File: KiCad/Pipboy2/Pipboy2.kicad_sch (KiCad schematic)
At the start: 12 parts, among them J1 Battery Socket, J2 LCD Socket, SW1 SW_SPST, SW2 SW_SPST

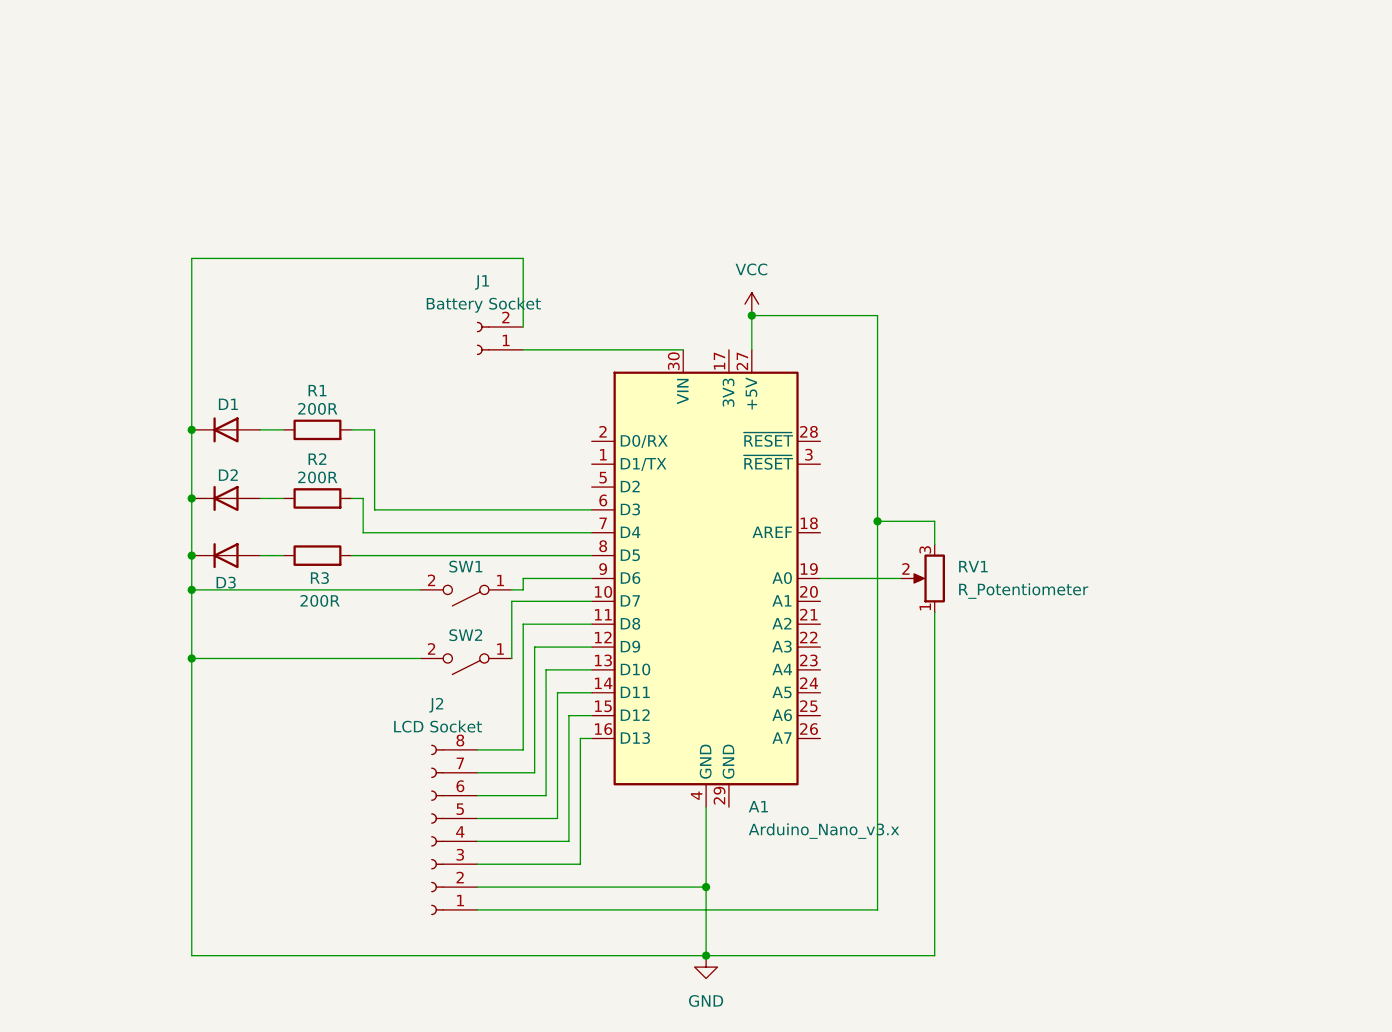
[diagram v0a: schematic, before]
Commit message: Added voltage reg, power button, updated pcb editor scheme
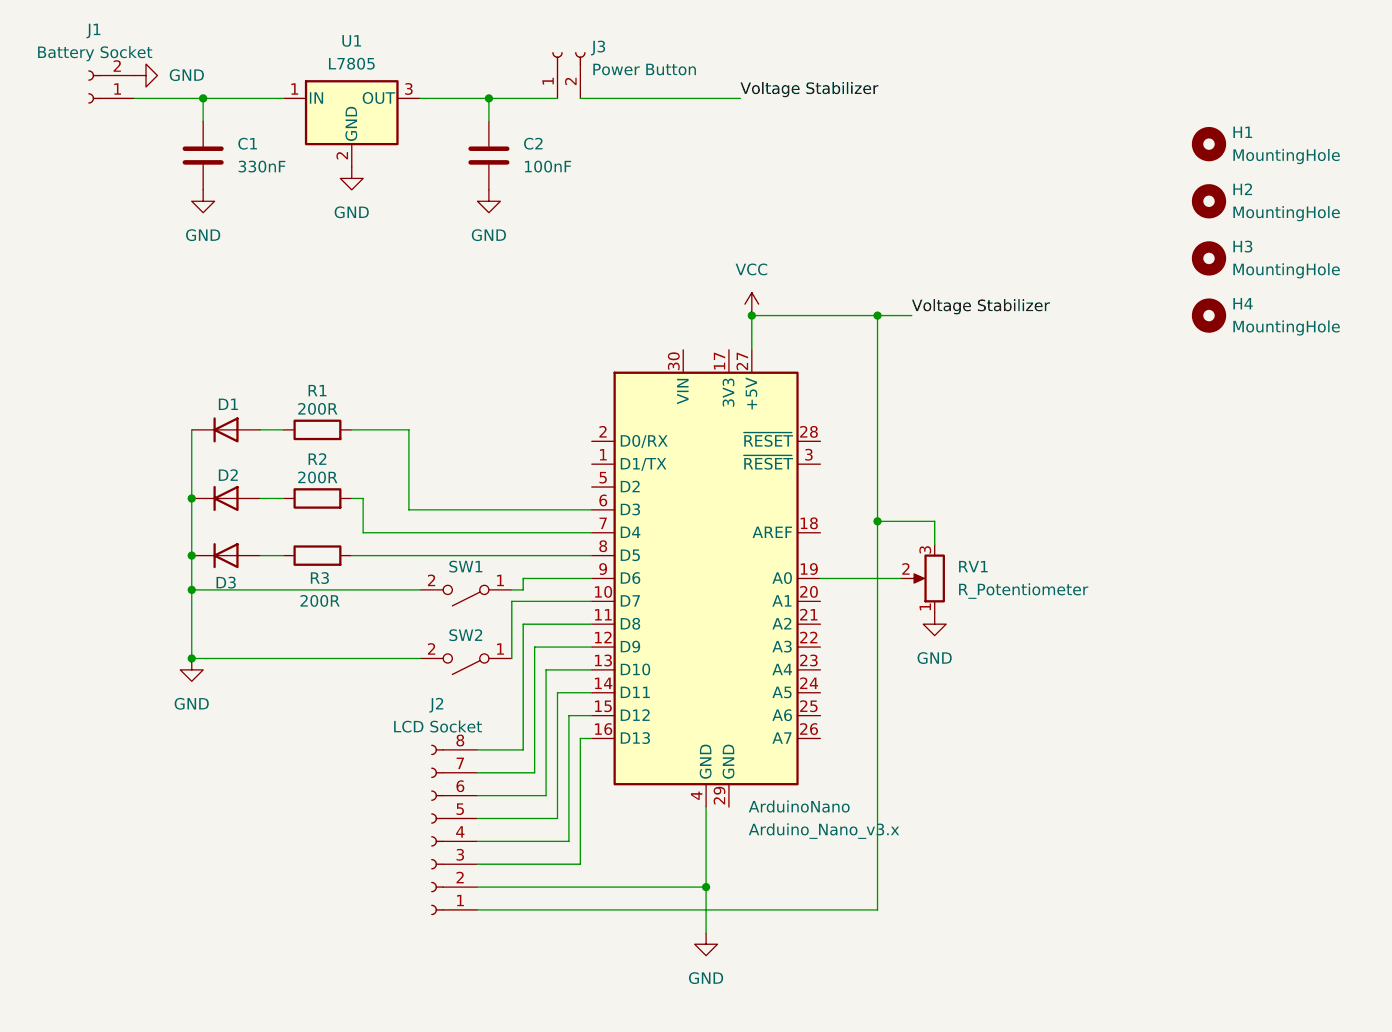
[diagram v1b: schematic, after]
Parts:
- added C1: 330nF, Capacitor_THT:CP_Axial_L10.0mm_D4.5mm_P15.00mm_Horizontal, symbol Device:C
- added C2: 100nF, Capacitor_THT:CP_Axial_L10.0mm_D4.5mm_P15.00mm_Horizontal, symbol Device:C
- added H1, H2, H3, H4: MountingHole, MountingHole:MountingHole_3.2mm_M3, symbol Mechanical:MountingHole
- added J3: Power Button, Connector_PinHeader_1.00mm:PinHeader_1x02_P1.00mm_Vertical, symbol Connector:Conn_01x02_Socket
- added U1: L7805, Package_TO_SOT_THT:TO-220-3_Vertical, symbol Regulator_Linear:L7805
- renumbered A1 to ArduinoNano
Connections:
- net GND: now also C1.2, C2.2, U1.2 (GND)
- net VCC: now also J3.2 (Pin_2)
- net at ArduinoNano.30 (VIN): no longer J1.1 (Pin_1)
- new net: C1.1, J1.1 (Pin_1), U1.1 (IN)
- new net: C2.1, J3.1 (Pin_1), U1.3 (OUT)
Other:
- moved on the sheet: J1

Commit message: Removed plate violations
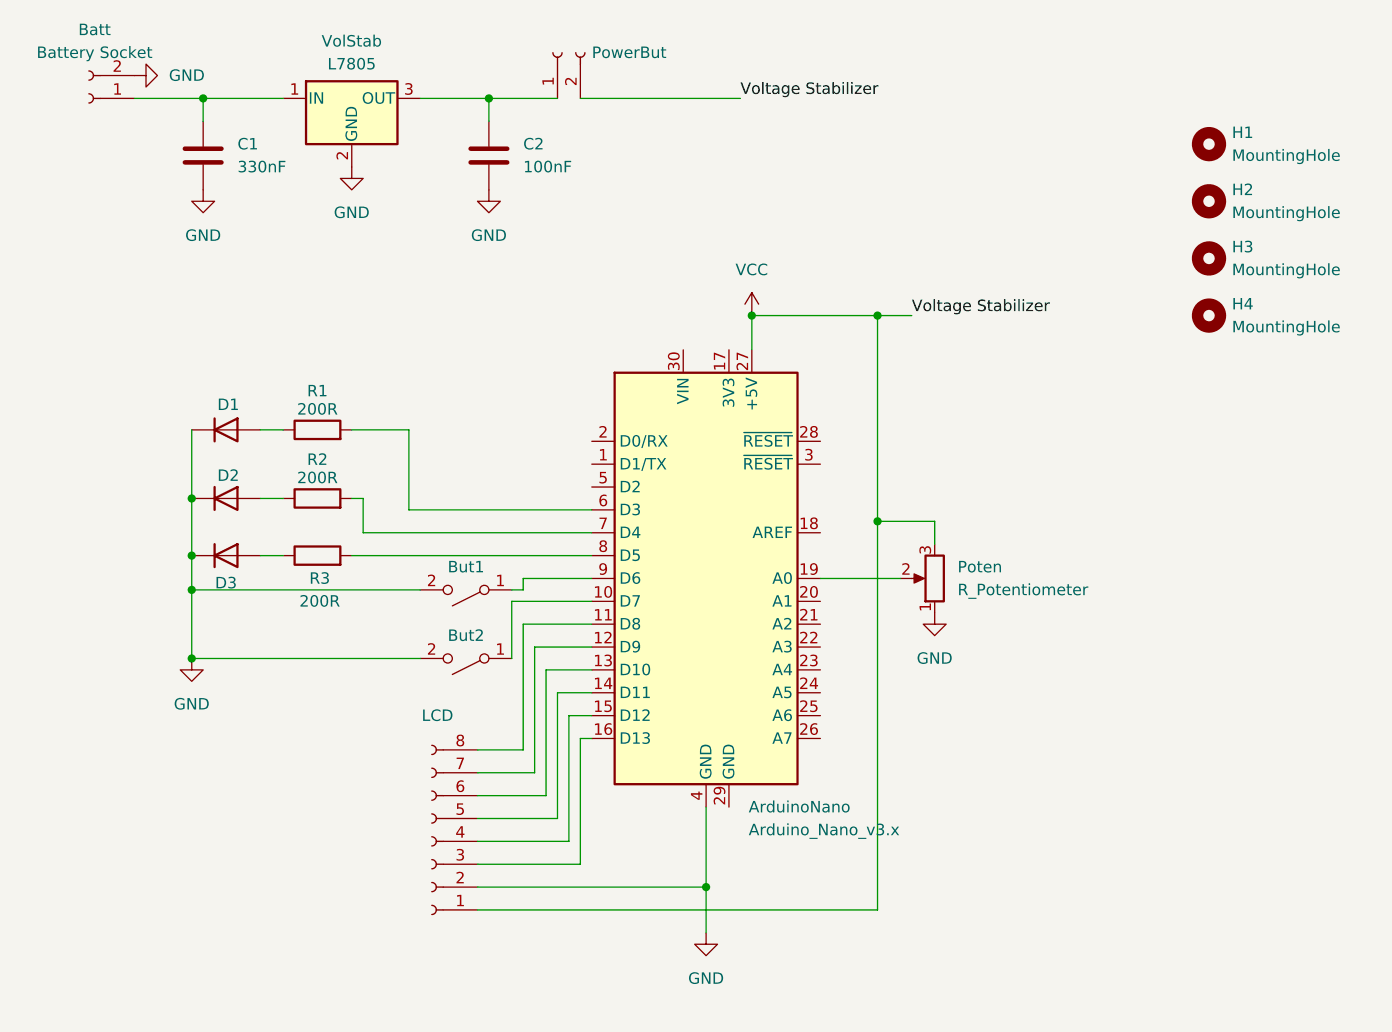
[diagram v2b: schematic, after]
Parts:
- LCD: renamed from J2; value LCD Socket -> ~
- PowerBut: renamed from J3; value Power Button -> ~; footprint Connector_PinHeader_1.00mm:PinHeader_1x02_P1.00mm_Vertical -> Connector_PinHeader_2.54mm:PinHeader_1x02_P2.54mm_Vertical
- renumbered J1 to Batt, SW1 to But1, SW2 to But2, RV1 to Poten, U1 to VolStab
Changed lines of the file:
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@@
 		(dnp no)
 		(fields_autoplaced yes)
-		(property "Reference" "U1"
+		(property "Reference" "VolStab"
 			(at 143.51 36.83 0)
 			(effects
@@
 			(project ""
 				(path "/e5f66db8-0cc8-44f6-bfd7-85690320585e"
-					(reference "U1")
+					(reference "VolStab")
 					(unit 1)
 				)
@@
 		(dnp no)
 		(fields_autoplaced yes)
-		(property "Reference" "SW2"
+		(property "Reference" "But2"
 			(at 156.21 102.87 0)
 			(effects
@@
 			(project "Pipboy2"
 				(path "/e5f66db8-0cc8-44f6-bfd7-85690320585e"
-					(reference "SW2")
+					(reference "But2")
 					(unit 1)
 				)
@@
 		(dnp no)
 		(fields_autoplaced yes)
-		(property "Reference" "J2"
-			(at 153.035 110.49 0)
-			(effects
-				(font
-					(size 1.27 1.27)
-				)
-			)
-		)
-		(property "Value" "LCD Socket"
+		(property "Reference" "LCD"
+			(at 153.035 111.76 0)
+			(effects
+				(font
+					(size 1.27 1.27)
+				)
+			)
+		)
+		(property "Value" "~"
 			(at 153.035 113.03 0)
 			(effects
@@
 			(project ""
 				(path "/e5f66db8-0cc8-44f6-bfd7-85690320585e"
-					(reference "J2")
+					(reference "LCD")
 					(unit 1)
 				)
@@
 		(dnp no)
 		(fields_autoplaced yes)
-		(property "Reference" "J1"
+		(property "Reference" "Batt"
 			(at 114.935 35.56 0)
 			(effects
@@
 			(project ""
 				(path "/e5f66db8-0cc8-44f6-bfd7-85690320585e"
-					(reference "J1")
+					(reference "Batt")
 					(unit 1)
 				)
@@
 		(dnp no)
 		(fields_autoplaced yes)
-		(property "Reference" "RV1"
+		(property "Reference" "Poten"
 			(at 210.82 95.2499 0)
 			(effects
@@
 			(project ""
 				(path "/e5f66db8-0cc8-44f6-bfd7-85690320585e"
-					(reference "RV1")
+					(reference "Poten")
 					(unit 1)
 				)
@@
 		(dnp no)
 		(fields_autoplaced yes)
-		(property "Reference" "J3"
-			(at 170.18 37.4649 90)
+		(property "Reference" "PowerBut"
+			(at 170.18 38.0999 90)
 			(effects
 				(font
@@
 			)
 		)
-		(property "Value" "Power Button"
-			(at 170.18 40.0049 90)
+		(property "Value" "~"
+			(at 170.18 40.005 90)
 			(effects
 				(font
@@
 			)
 		)
-		(property "Footprint" "Connector_PinHeader_1.00mm:PinHeader_1x02_P1.00mm_Vertical"
+		(property "Footprint" "Connector_PinHeader_2.54mm:PinHeader_1x02_P2.54mm_Vertical"
 			(at 166.37 38.1 0)
 			(effects
@@
 			(project "Pipboy2"
 				(path "/e5f66db8-0cc8-44f6-bfd7-85690320585e"
-					(reference "J3")
+					(reference "PowerBut")
 					(unit 1)
 				)
@@
 		(dnp no)
 		(fields_autoplaced yes)
-		(property "Reference" "SW1"
+		(property "Reference" "But1"
 			(at 156.21 95.25 0)
 			(effects
@@
 			(project ""
 				(path "/e5f66db8-0cc8-44f6-bfd7-85690320585e"
-					(reference "SW1")
-					(unit 1)
-				)
+					(reference "But1")
+					(unit 1)
+				)

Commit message: Exported steps
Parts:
- renumbered ArduinoNano to ArduinoNano1, Batt to Batt1, LCD to LCD1, Poten to Poten1, PowerBut to PowerBut1, VolStab to VolStab1
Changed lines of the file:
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@@
 		(dnp no)
 		(fields_autoplaced yes)
-		(property "Reference" "ArduinoNano"
+		(property "Reference" "ArduinoNano1"
 			(at 187.6141 121.92 0)
 			(effects
@@
 			(project ""
 				(path "/e5f66db8-0cc8-44f6-bfd7-85690320585e"
-					(reference "ArduinoNano")
+					(reference "ArduinoNano1")
 					(unit 1)
 				)
@@
 		(dnp no)
 		(fields_autoplaced yes)
-		(property "Reference" "VolStab"
+		(property "Reference" "VolStab1"
 			(at 143.51 36.83 0)
 			(effects
@@
 			(project ""
 				(path "/e5f66db8-0cc8-44f6-bfd7-85690320585e"
-					(reference "VolStab")
+					(reference "VolStab1")
 					(unit 1)
 				)
@@
 		(dnp no)
 		(fields_autoplaced yes)
-		(property "Reference" "LCD"
+		(property "Reference" "LCD1"
 			(at 153.035 111.76 0)
 			(effects
@@
 			(project ""
 				(path "/e5f66db8-0cc8-44f6-bfd7-85690320585e"
-					(reference "LCD")
+					(reference "LCD1")
 					(unit 1)
 				)
@@
 		(dnp no)
 		(fields_autoplaced yes)
-		(property "Reference" "Batt"
+		(property "Reference" "Batt1"
 			(at 114.935 35.56 0)
 			(effects
@@
 			(project ""
 				(path "/e5f66db8-0cc8-44f6-bfd7-85690320585e"
-					(reference "Batt")
+					(reference "Batt1")
 					(unit 1)
 				)
@@
 		(dnp no)
 		(fields_autoplaced yes)
-		(property "Reference" "Poten"
+		(property "Reference" "Poten1"
 			(at 210.82 95.2499 0)
 			(effects
@@
 			(project ""
 				(path "/e5f66db8-0cc8-44f6-bfd7-85690320585e"
-					(reference "Poten")
+					(reference "Poten1")
 					(unit 1)
 				)
@@
 		(dnp no)
 		(fields_autoplaced yes)
-		(property "Reference" "PowerBut"
+		(property "Reference" "PowerBut1"
 			(at 170.18 38.0999 90)
 			(effects
@@
 			(project "Pipboy2"
 				(path "/e5f66db8-0cc8-44f6-bfd7-85690320585e"
-					(reference "PowerBut")
-					(unit 1)
-				)
+					(reference "PowerBut1")
+					(unit 1)
+				)
